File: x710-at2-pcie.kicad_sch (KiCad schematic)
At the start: 16 parts, among them J7 Tag-Connect_TC2050-IDC-NL_2x5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, U9 EZX710AT2_S_LMR5

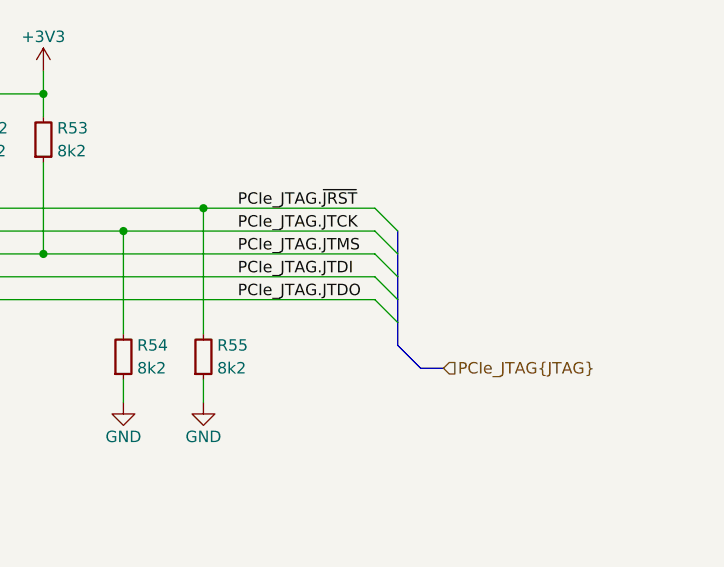
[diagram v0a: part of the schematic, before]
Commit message: [#86617] Power U10 from OCuLink, remove JTAG sheet pin, fix I2C cross
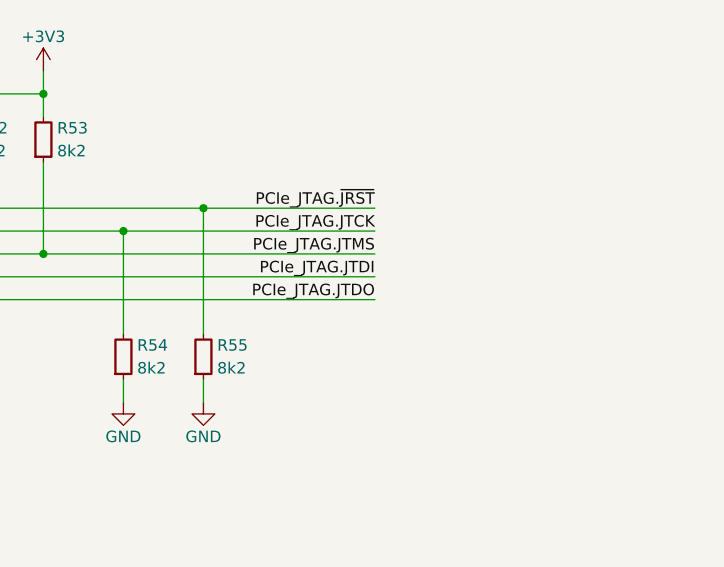
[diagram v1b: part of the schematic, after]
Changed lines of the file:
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@@
-	)
-	(bus_entry
-		(at 293.37 97.79)
-		(size -2.54 -2.54)
-		(stroke
-			(width 0)
-			(type default)
-		)
 	)
 	(bus_entry
@@
 	)
 	(bus_entry
-		(at 293.37 95.25)
-		(size -2.54 -2.54)
-		(stroke
-			(width 0)
-			(type default)
-		)
-	)
-	(bus_entry
 		(at 140.97 107.95)
 		(size 2.54 -2.54)
@@
 	)
 	(bus_entry
-		(at 293.37 90.17)
-		(size -2.54 -2.54)
-		(stroke
-			(width 0)
-			(type default)
-		)
-	)
-	(bus_entry
-		(at 293.37 92.71)
-		(size -2.54 -2.54)
-		(stroke
-			(width 0)
-			(type default)
-		)
-	)
-	(bus_entry
 		(at 140.97 113.03)
 		(size 2.54 -2.54)
@@
 	)
 	(bus_entry
-		(at 293.37 100.33)
-		(size -2.54 -2.54)
-		(stroke
-			(width 0)
-			(type default)
-		)
-	)
-	(bus_entry
 		(at 140.97 135.89)
 		(size 2.54 -2.54)
@@
 	(bus
 		(pts
-			(xy 293.37 100.33) (xy 293.37 102.87)
-		)
-		(stroke
-			(width 0)
-			(type default)
-		)
-	)
-	(bus
-		(pts
 			(xy 140.97 138.43) (xy 140.97 143.51)
 		)
@@
 		)
 	)
-	(bus
-		(pts
-			(xy 295.91 105.41) (xy 298.45 105.41)
-		)
-		(stroke
-			(width 0)
-			(type default)
-		)
-	)
 	(wire
 		(pts
@@
 	(bus
 		(pts
-			(xy 293.37 92.71) (xy 293.37 95.25)
-		)
-		(stroke
-			(width 0)
-			(type default)
-		)
-	)
-	(bus
-		(pts
 			(xy 140.97 120.65) (xy 140.97 123.19)
 		)
@@
 		)
 	)
-	(bus
-		(pts
-			(xy 295.91 105.41) (xy 293.37 102.87)
-		)
-		(stroke
-			(width 0)
-			(type default)
-		)
-	)
 	(wire
 		(pts
@@
 		)
 	)
-	(bus
-		(pts
-			(xy 293.37 97.79) (xy 293.37 100.33)
-		)
-		(stroke
-			(width 0)
-			(type default)
-		)
-	)
 	(wire
 		(pts
@@
 		(pts
 			(xy 233.68 95.25) (xy 245.11 95.25)
-		)
-		(stroke
-			(width 0)
-			(type default)
-		)
-	)
-	(bus
-		(pts
-			(xy 293.37 95.25) (xy 293.37 97.79)
-		)
-		(stroke
-			(width 0)
-			(type default)
-		)
-	)
-	(bus
-		(pts
-			(xy 293.37 90.17) (xy 293.37 92.71)
 		)
 		(stroke
@@
 	)
 	(label "PCIe_JTAG.~{JRST}"
-		(at 275.59 87.63 0)
-		(effects
-			(font
-				(size 1.27 1.27)
-			)
-			(justify left bottom)
+		(at 290.83 87.63 180)
+		(effects
+			(font
+				(size 1.27 1.27)
+			)
+			(justify right bottom)
 		)
 	)
 	(label "PCIe_JTAG.JTDI"
-		(at 275.59 95.25 0)
-		(effects
-			(font
-				(size 1.27 1.27)
-			)
-			(justify left bottom)
+		(at 290.83 95.25 180)
+		(effects
+			(font
+				(size 1.27 1.27)
+			)
+			(justify right bottom)
 		)
 	)
@@
 	)
 	(label "PCIe_JTAG.JTMS"
-		(at 275.59 92.71 0)
-		(effects
-			(font
-				(size 1.27 1.27)
-			)
-			(justify left bottom)
+		(at 290.83 92.71 180)
+		(effects
+			(font
+				(size 1.27 1.27)
+			)
+			(justify right bottom)
 		)
 	)
@@
 	)
 	(label "PCIe_JTAG.JTCK"
-		(at 275.59 90.17 0)
-		(effects
-			(font
-				(size 1.27 1.27)
-			)
-			(justify left bottom)
+		(at 290.83 90.17 180)
+		(effects
+			(font
+				(size 1.27 1.27)
+			)
+			(justify right bottom)
 		)
 	)
@@
 	)
 	(label "PCIe_JTAG.JTDO"
-		(at 275.59 97.79 0)
-		(effects
-			(font
-				(size 1.27 1.27)
-			)
-			(justify left bottom)
+		(at 290.83 97.79 180)
+		(effects
+			(font
+				(size 1.27 1.27)
+			)
+			(justify right bottom)
 		)
 	)
@@
 		)
 	)
-	(hierarchical_label "PCIe_JTAG{JTAG}"
-		(shape input)
-		(at 298.45 105.41 0)
-		(effects
-			(font
-				(size 1.27 1.27)
-			)
-			(justify left)
-		)
-	)

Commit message: [#86351] Rename project
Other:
- title: 10GbE Expansion -> OCuLink to 10GbE adapter
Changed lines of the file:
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@@
 	(paper "A3")
 	(title_block
-		(title "10GbE Expansion")
+		(title "OCuLink to 10GbE adapter")
 		(date "2025-11-07")
 		(rev "1.0.0")
@@
 		)
 		(instances
-			(project "10-gbe-expansion"
+			(project "OCuLink to 10GbE adapter"
 				(path "/04bda987-e5eb-48b4-9e90-d8211dc11b39/2e3e9f9b-8e60-4e62-87df-aa866913a2fb"
 					(reference "R53")
@@
 		)
 		(instances
-			(project "10-gbe-expansion"
+			(project "OCuLink to 10GbE adapter"
 				(path "/04bda987-e5eb-48b4-9e90-d8211dc11b39/2e3e9f9b-8e60-4e62-87df-aa866913a2fb"
 					(reference "C196")
@@
 		)
 		(instances
-			(project "10-gbe-expansion"
+			(project "OCuLink to 10GbE adapter"
 				(path "/04bda987-e5eb-48b4-9e90-d8211dc11b39/2e3e9f9b-8e60-4e62-87df-aa866913a2fb"
 					(reference "#PWR0245")
@@
 		)
 		(instances
-			(project "10-gbe-expansion"
+			(project "OCuLink to 10GbE adapter"
 				(path "/04bda987-e5eb-48b4-9e90-d8211dc11b39/2e3e9f9b-8e60-4e62-87df-aa866913a2fb"
 					(reference "R56")
@@
 		)
 		(instances
-			(project "10-gbe-expansion"
+			(project "OCuLink to 10GbE adapter"
 				(path "/04bda987-e5eb-48b4-9e90-d8211dc11b39/2e3e9f9b-8e60-4e62-87df-aa866913a2fb"
 					(reference "C194")
@@
 		)
 		(instances
-			(project "10-gbe-expansion"
+			(project "OCuLink to 10GbE adapter"
 				(path "/04bda987-e5eb-48b4-9e90-d8211dc11b39/2e3e9f9b-8e60-4e62-87df-aa866913a2fb"
 					(reference "C195")
@@
 		)
 		(instances
-			(project "10-gbe-expansion"
+			(project "OCuLink to 10GbE adapter"
 				(path "/04bda987-e5eb-48b4-9e90-d8211dc11b39/2e3e9f9b-8e60-4e62-87df-aa866913a2fb"
 					(reference "R52")
@@
 		)
 		(instances
-			(project "10-gbe-expansion"
+			(project "OCuLink to 10GbE adapter"
 				(path "/04bda987-e5eb-48b4-9e90-d8211dc11b39/2e3e9f9b-8e60-4e62-87df-aa866913a2fb"
 					(reference "C191")
@@
 		)
 		(instances
-			(project "10-gbe-expansion"
+			(project "OCuLink to 10GbE adapter"
 				(path "/04bda987-e5eb-48b4-9e90-d8211dc11b39/2e3e9f9b-8e60-4e62-87df-aa866913a2fb"
 					(reference "R55")
@@
 		)
 		(instances
-			(project "10-gbe-expansion"
+			(project "OCuLink to 10GbE adapter"
 				(path "/04bda987-e5eb-48b4-9e90-d8211dc11b39/2e3e9f9b-8e60-4e62-87df-aa866913a2fb"
 					(reference "#PWR0246")
@@
 		)
 		(instances
-			(project "10-gbe-expansion"
+			(project "OCuLink to 10GbE adapter"
 				(path "/04bda987-e5eb-48b4-9e90-d8211dc11b39/2e3e9f9b-8e60-4e62-87df-aa866913a2fb"
 					(reference "C193")
@@
 		)
 		(instances
-			(project "10-gbe-expansion"
+			(project "OCuLink to 10GbE adapter"
 				(path "/04bda987-e5eb-48b4-9e90-d8211dc11b39/2e3e9f9b-8e60-4e62-87df-aa866913a2fb"
 					(reference "C190")
@@
 		)
 		(instances
-			(project "10-gbe-expansion"
+			(project "OCuLink to 10GbE adapter"
 				(path "/04bda987-e5eb-48b4-9e90-d8211dc11b39/2e3e9f9b-8e60-4e62-87df-aa866913a2fb"
 					(reference "C192")
@@
 		)
 		(instances
-			(project "10-gbe-expansion"
+			(project "OCuLink to 10GbE adapter"
 				(path "/04bda987-e5eb-48b4-9e90-d8211dc11b39/2e3e9f9b-8e60-4e62-87df-aa866913a2fb"
 					(reference "#PWR0247")
@@
 		)
 		(instances
-			(project "10-gbe-expansion"
+			(project "OCuLink to 10GbE adapter"
 				(path "/04bda987-e5eb-48b4-9e90-d8211dc11b39/2e3e9f9b-8e60-4e62-87df-aa866913a2fb"
 					(reference "#PWR0248")
@@
 		)
 		(instances
-			(project "10-gbe-expansion"
+			(project "OCuLink to 10GbE adapter"
 				(path "/04bda987-e5eb-48b4-9e90-d8211dc11b39/2e3e9f9b-8e60-4e62-87df-aa866913a2fb"
 					(reference "#PWR0249")
@@
 		)
 		(instances
-			(project "10-gbe-expansion"
+			(project "OCuLink to 10GbE adapter"
 				(path "/04bda987-e5eb-48b4-9e90-d8211dc11b39/2e3e9f9b-8e60-4e62-87df-aa866913a2fb"
 					(reference "C197")
@@
 		)
 		(instances
-			(project "10-gbe-expansion"
+			(project "OCuLink to 10GbE adapter"
 				(path "/04bda987-e5eb-48b4-9e90-d8211dc11b39/2e3e9f9b-8e60-4e62-87df-aa866913a2fb"
 					(reference "U9")

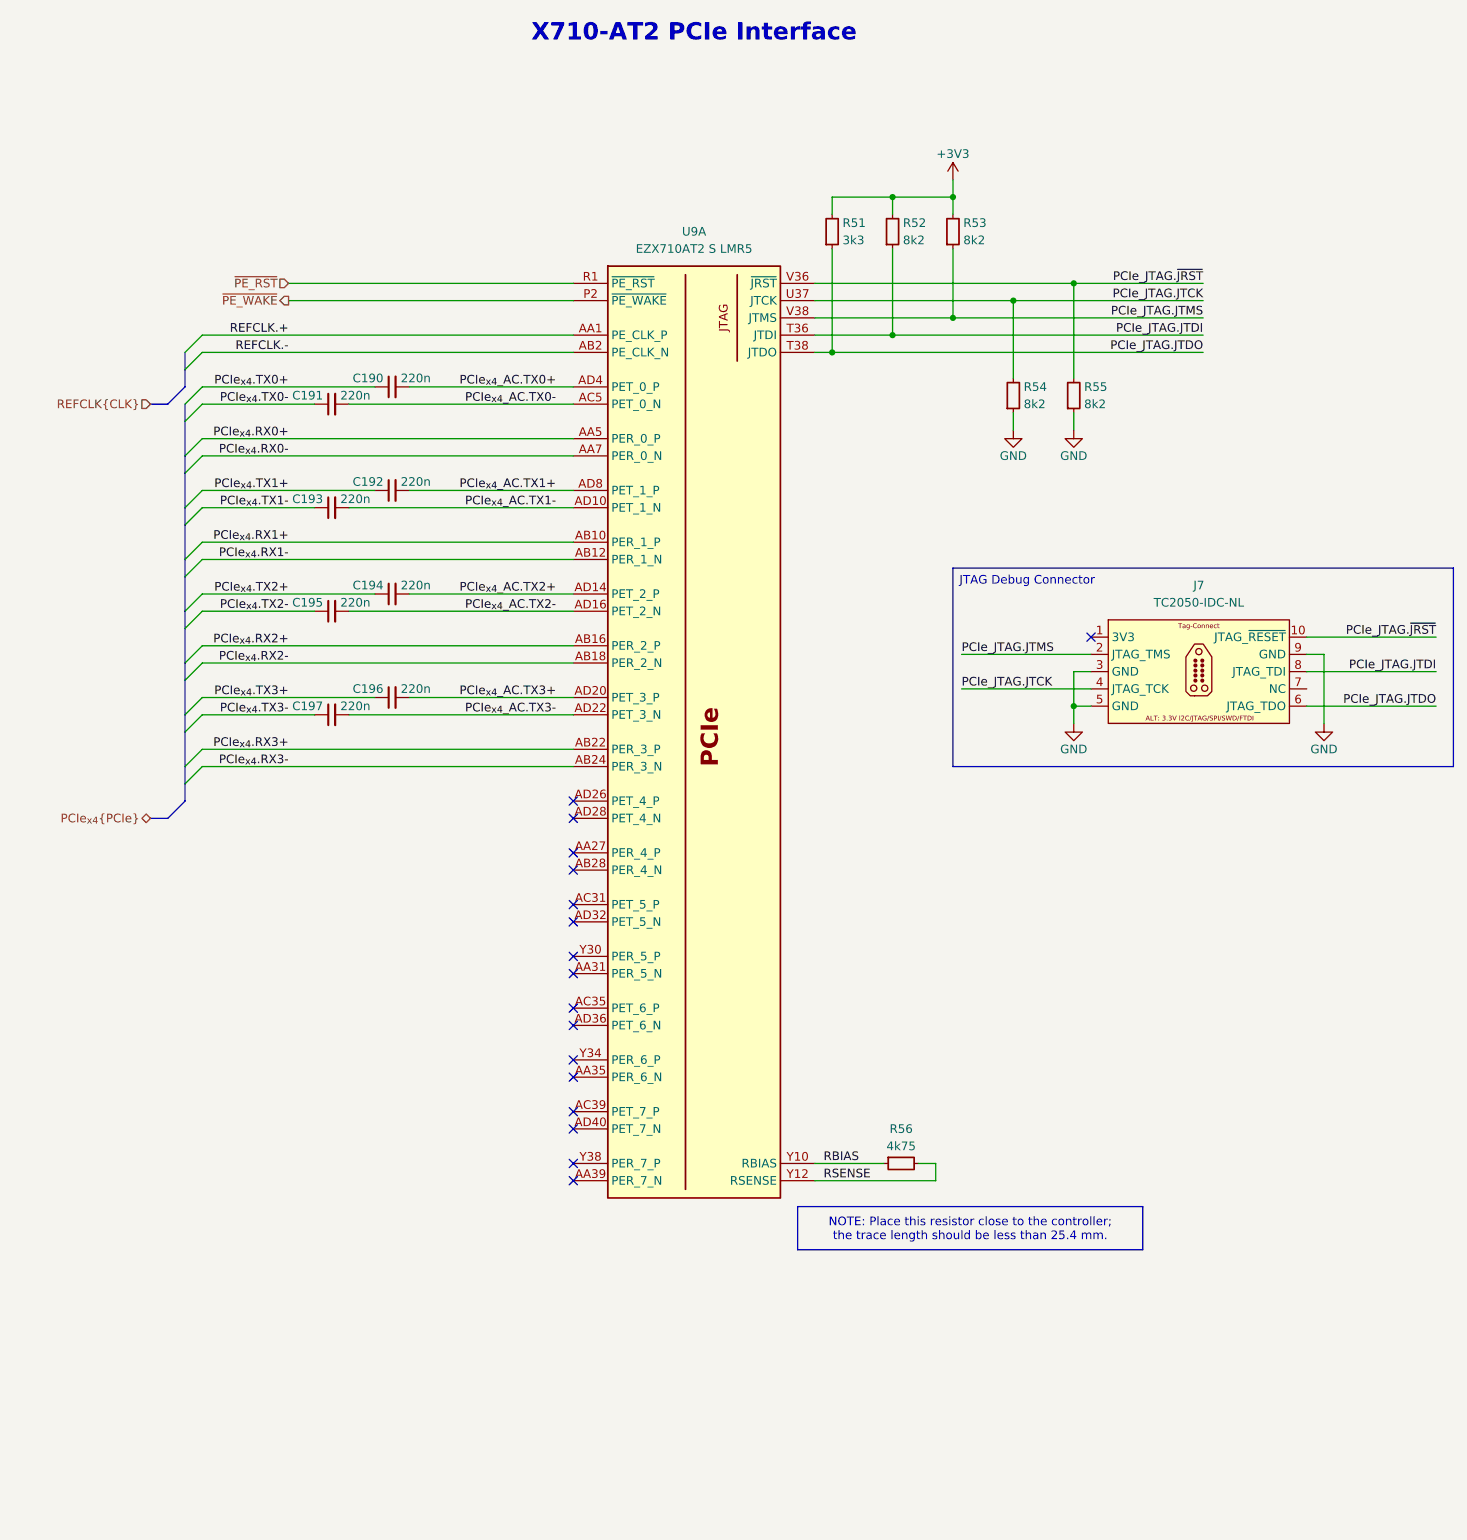
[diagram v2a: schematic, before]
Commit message: [#88407] Sch: Add PCIe ref clock; Add ICT testpoints; Add fan TVS
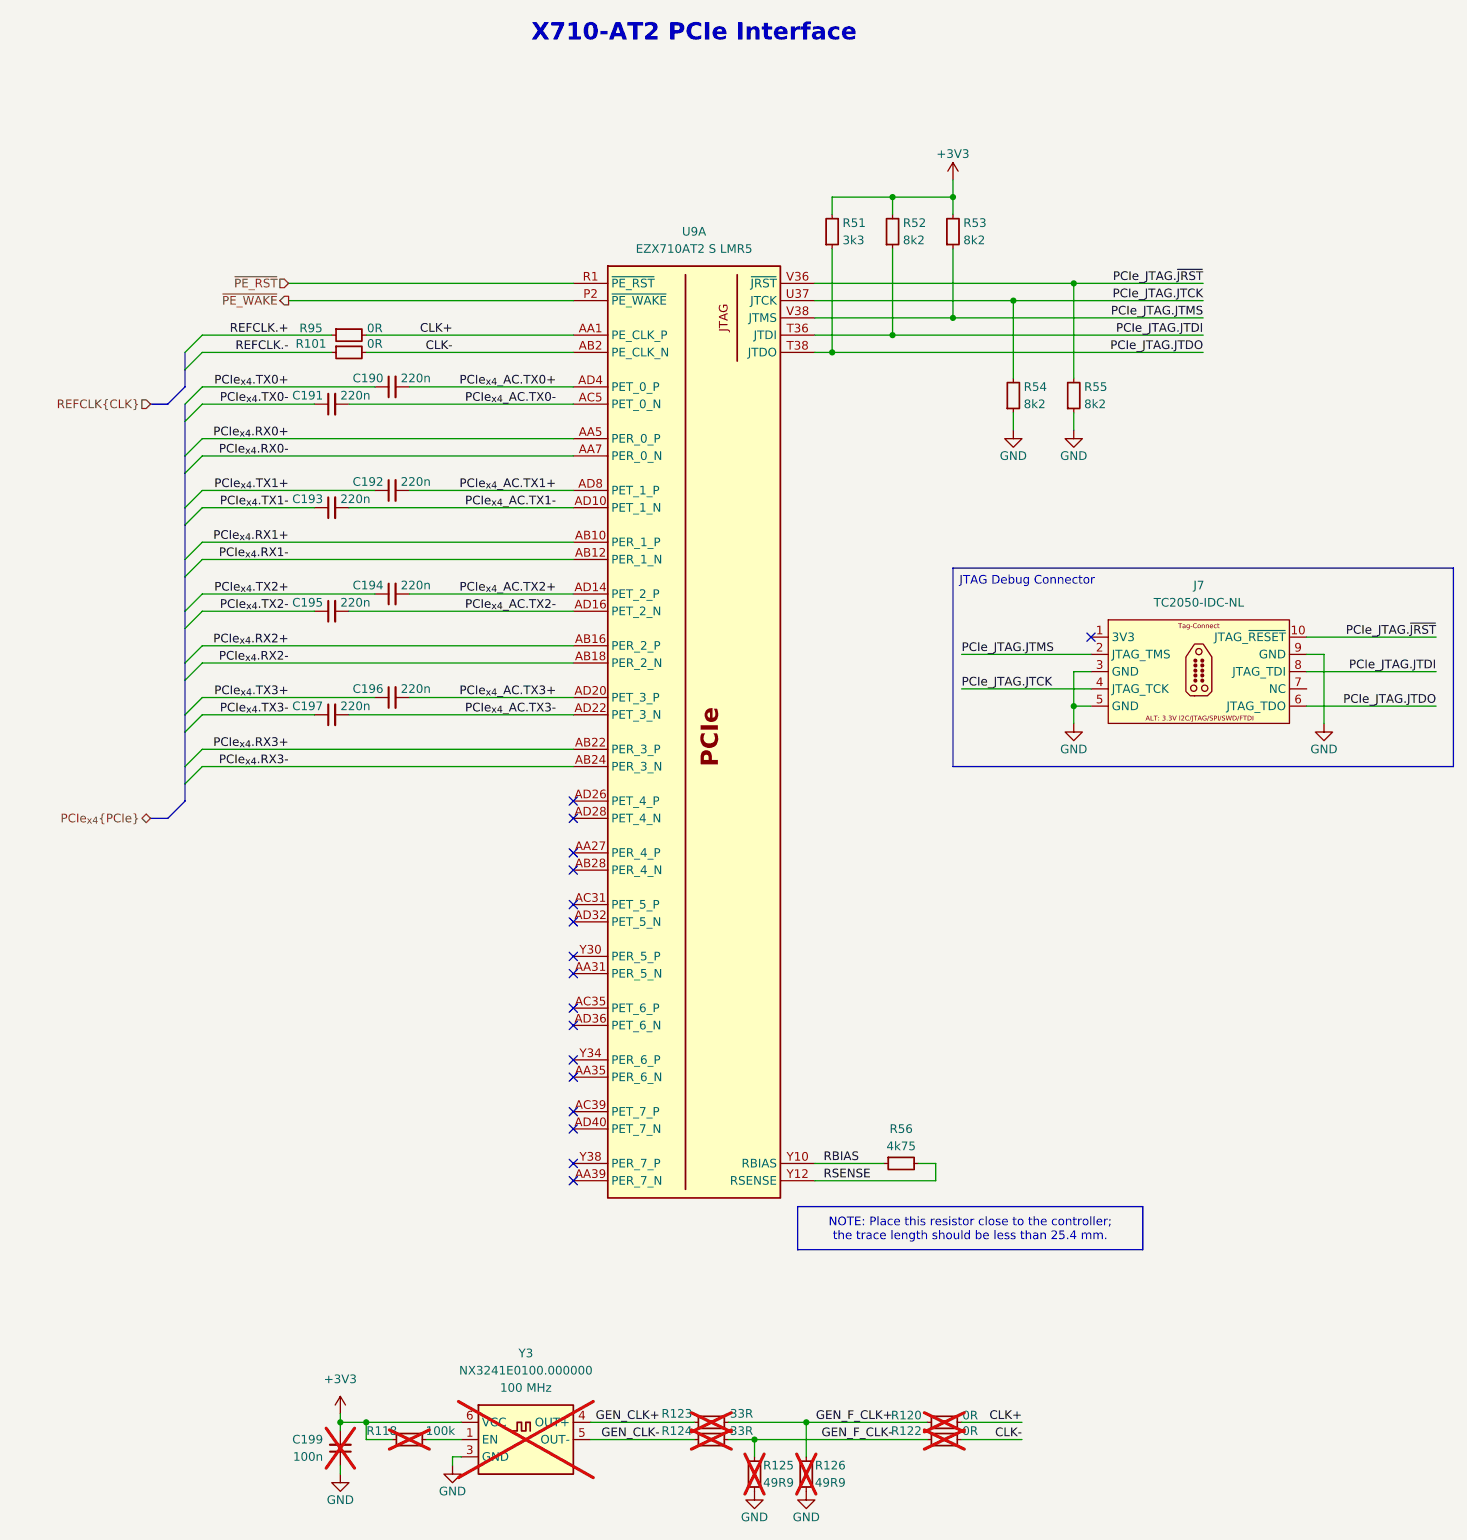
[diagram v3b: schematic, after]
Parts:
- added C199: C_100n_0402, antmicro-footprints:C_0402_1005Metric, symbol antmicroCapacitors0402:C_100n_0402
- added R101, R120, R122, R95: R_0R_0402, antmicro-footprints:R_0402_1005Metric, symbol antmicroResistors0402:R_0R_0402
- added R118: R_100k_0402, antmicro-footprints:R_0402_1005Metric, symbol antmicroResistors0402:R_100k_0402
- added R123, R124: R_33R_0402, antmicro-footprints:R_0402_1005Metric, symbol antmicroResistors0402:R_33R_0402
- added R125, R126: R_49R9_0402, antmicro-footprints:R_0402_1005Metric, symbol antmicroResistors0402:R_49R9_0402
- added Y3: Oscillator_100MHz_NX324, antmicro-footprints:Oscillator_SMD_Abracon_AX3_3.2x2.5x1mm, symbol antmicroOscillators:Oscillator_100MHz_NX324
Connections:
- net +3V3: now also C199.2, R118.1, Y3.6 (VCC)
- net GND: now also C199.1, R125.1, R126.1, Y3.3 (GND)
- net REFCLK.+: now also R95.1; no longer U9.AA1 (PE_CLK_P)
- net REFCLK.-: now also R101.1; no longer U9.AB2 (PE_CLK_N)
- new net: R118.2, Y3.1 (EN)
- new net CLK+: R120.2, R95.2, U9.AA1 (PE_CLK_P)
- new net CLK-: R101.2, R122.2, U9.AB2 (PE_CLK_N)
- new net GEN_CLK+: R123.1, Y3.4 (OUT+)
- new net GEN_CLK-: R124.1, Y3.5 (OUT-)
- new net GEN_F_CLK+: R120.1, R123.2, R126.2
- new net GEN_F_CLK-: R122.1, R124.2, R125.2
